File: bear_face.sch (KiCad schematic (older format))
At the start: 276 parts, among them J1 USB_B_Micro, Q1 2N7002, SW1 SW_Push, U1 ATmega32U4-AU, U2 SRV05-4, Y1 16MHz

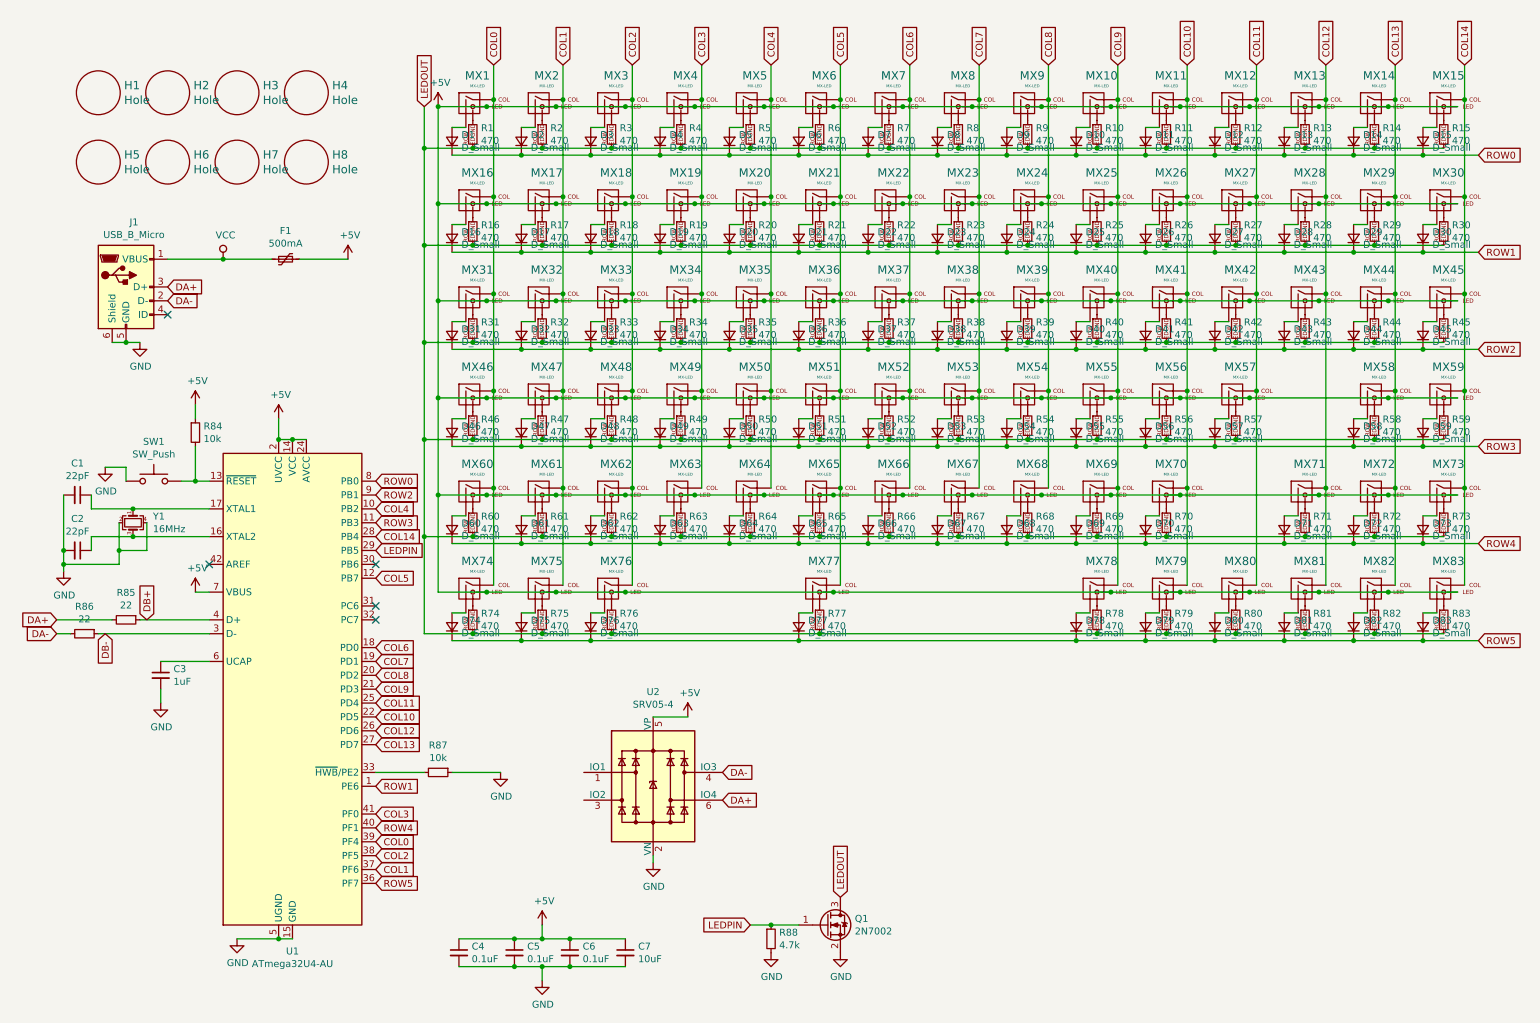
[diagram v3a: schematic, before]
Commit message: AVR ISP pins added, routed
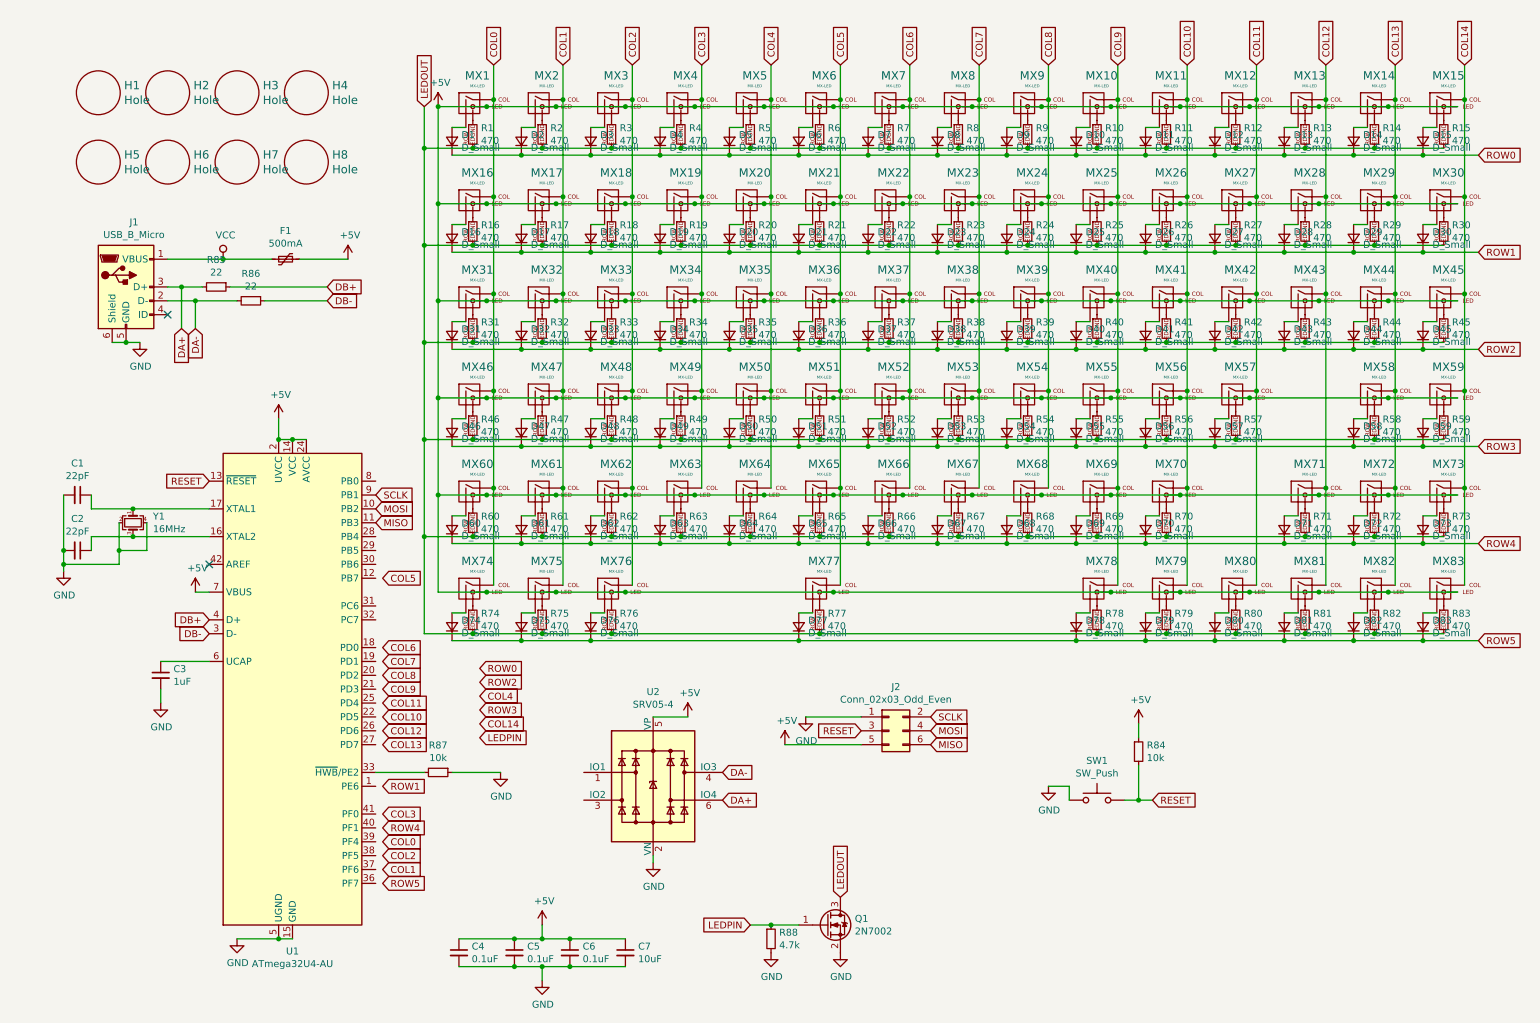
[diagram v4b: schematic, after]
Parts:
- added J2: Conn_02x03_Odd_Even, Connector_PinSocket_2.54mm:PinSocket_2x03_P2.54mm_Vertical, symbol Connector_Generic:Conn_02x03_Odd_Even
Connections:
- net +5V: now also J2.5 (Pin_5)
- net COL0: no longer U1.39 (PF4)
- net COL1: no longer U1.37 (PF6)
- net COL10: no longer U1.22 (PD5)
- net COL11: no longer U1.25 (PD4)
- net COL12: no longer U1.26 (PD6)
- net COL13: no longer U1.27 (PD7)
- net COL14: no longer U1.28 (PB4)
- net COL2: no longer U1.38 (PF5)
- net COL3: no longer U1.41 (PF0)
- net COL4: no longer U1.10 (PB2)
- net COL5: no longer U1.12 (PB7)
- net COL6: no longer U1.18 (PD0)
- net COL7: no longer U1.19 (PD1)
- net COL8: no longer U1.20 (PD2)
- net COL9: no longer U1.21 (PD3)
- net GND: now also J2.1 (Pin_1)
- net LEDPIN: no longer U1.29 (PB5)
- net ROW0: no longer U1.8 (PB0)
- net ROW1: no longer U1.1 (PE6)
- net ROW2: no longer U1.9 (PB1)
- net ROW3: no longer U1.11 (PB3)
- net ROW4: no longer U1.40 (PF1)
- net ROW5: no longer U1.36 (PF7)
- net RESET: now reaches R84.2, SW1.2, U1.13 (~RESET)
- net RESET: now also J2.3 (Pin_3)
- new net MISO: J2.6 (Pin_6), U1.11 (PB3)
- new net MOSI: J2.4 (Pin_4), U1.10 (PB2)
- new net SCLK: J2.2 (Pin_2), U1.9 (PB1)
- no-connect marks 5 -> 2
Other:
- moved on the sheet: R84, R85, R86, SW1
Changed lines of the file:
@@
 	1    0    0    -1
 $EndComp
-Text GLabel 1500 2500 2    50   Input ~ 0
+Text GLabel 1700 2700 3    50   Input ~ 0
 DA-
-Text GLabel 1500 2400 2    50   Input ~ 0
+Text GLabel 1600 2700 3    50   Input ~ 0
 DA+
 $Comp
@@
 L Device:R_Small R85
 U 1 1 5E2BAE37
-P 1200 4800
-F 0 "R85" V 1004 4800 50  0000 C CNN
-F 1 "22" V 1095 4800 50  0000 C CNN
-F 2 "Resistor_SMD:R_0805_2012Metric_Pad1.15x1.40mm_HandSolder" H 1200 4800 50  0001 C CNN
-F 3 "~" H 1200 4800 50  0001 C CNN
-	1    1200 4800
+P 1850 2400
+F 0 "R85" V 1654 2400 50  0000 C CNN
+F 1 "22" V 1745 2400 50  0000 C CNN
+F 2 "Resistor_SMD:R_0805_2012Metric_Pad1.15x1.40mm_HandSolder" H 1850 2400 50  0001 C CNN
+F 3 "~" H 1850 2400 50  0001 C CNN
+	1    1850 2400
 	0    1    1    0
 $EndComp
@@
 L Device:R_Small R86
 U 1 1 5E2BDE9E
-P 900 4900
-F 0 "R86" V 704 4900 50  0000 C CNN
-F 1 "22" V 795 4900 50  0000 C CNN
-F 2 "Resistor_SMD:R_0805_2012Metric_Pad1.15x1.40mm_HandSolder" H 900 4900 50  0001 C CNN
-F 3 "~" H 900 4900 50  0001 C CNN
-	1    900  4900
+P 2100 2500
+F 0 "R86" V 1904 2500 50  0000 C CNN
+F 1 "22" V 1995 2500 50  0000 C CNN
+F 2 "Resistor_SMD:R_0805_2012Metric_Pad1.15x1.40mm_HandSolder" H 2100 2500 50  0001 C CNN
+F 3 "~" H 2100 2500 50  0001 C CNN
+	1    2100 2500
 	0    1    1    0
 $EndComp
-Wire Wire Line
-	800  4900 700  4900
-Wire Wire Line
-	700  4800 1100 4800
 $Comp
 L Device:C_Small C3
@@
 L Switch:SW_Push SW1
 U 1 1 5DFE33D6
-P 1400 3800
-F 0 "SW1" H 1400 4085 50  0000 C CNN
-F 1 "SW_Push" H 1400 3994 50  0000 C CNN
-F 2 "bear_face_parts:PushButton_6x6mm_TH_Pretty" H 1400 4000 50  0001 C CNN
-F 3 "~" H 1400 4000 50  0001 C CNN
-	1    1400 3800
+P 8200 6100
+F 0 "SW1" H 8200 6385 50  0000 C CNN
+F 1 "SW_Push" H 8200 6294 50  0000 C CNN
+F 2 "bear_face_parts:PushButton_6x6mm_TH_Pretty" H 8200 6300 50  0001 C CNN
+F 3 "~" H 8200 6300 50  0001 C CNN
+	1    8200 6100
 	1    0    0    -1
 $EndComp
@@
 	950  4200 950  4300
 Wire Wire Line
-	1600 3800 1700 3800
+	8400 6100 8500 6100
 $Comp
 L power:GND #PWR07
 U 1 1 5E709B12
-P 1050 3700
-F 0 "#PWR07" H 1050 3450 50  0001 C CNN
-F 1 "GND" H 1055 3527 50  0000 C CNN
-F 2 "" H 1050 3700 50  0001 C CNN
-F 3 "" H 1050 3700 50  0001 C CNN
-	1    1050 3700
-	1    0    0    -1
-$EndComp
-Wire Wire Line
-	1050 3700 1200 3700
-Wire Wire Line
-	1200 3700 1200 3800
+P 7850 6000
+F 0 "#PWR07" H 7850 5750 50  0001 C CNN
+F 1 "GND" H 7855 5827 50  0000 C CNN
+F 2 "" H 7850 6000 50  0001 C CNN
+F 3 "" H 7850 6000 50  0001 C CNN
+	1    7850 6000
+	1    0    0    -1
+$EndComp
+Wire Wire Line
+	7850 6000 8000 6000
+Wire Wire Line
+	8000 6000 8000 6100
 $Comp
 L Device:R_Small R84
 U 1 1 5E729BAE
-P 1700 3450
-F 0 "R84" H 1759 3496 50  0000 L CNN
-F 1 "10k" H 1759 3405 50  0000 L CNN
-F 2 "Resistor_SMD:R_0805_2012Metric_Pad1.15x1.40mm_HandSolder" H 1700 3450 50  0001 C CNN
-F 3 "~" H 1700 3450 50  0001 C CNN
-	1    1700 3450
-	1    0    0    -1
-$EndComp
-Wire Wire Line
-	1700 3550 1700 3800
-Connection ~ 1700 3800
-Wire Wire Line
-	1700 3800 1800 3800
+P 8500 5750
+F 0 "R84" H 8559 5796 50  0000 L CNN
+F 1 "10k" H 8559 5705 50  0000 L CNN
+F 2 "Resistor_SMD:R_0805_2012Metric_Pad1.15x1.40mm_HandSolder" H 8500 5750 50  0001 C CNN
+F 3 "~" H 8500 5750 50  0001 C CNN
+	1    8500 5750
+	1    0    0    -1
+$EndComp
+Wire Wire Line
+	8500 5850 8500 6100
+Connection ~ 8500 6100
+Wire Wire Line
+	8500 6100 8600 6100
 $Comp
 L power:+5V #PWR05
 U 1 1 5E749519
-P 1700 3250
-F 0 "#PWR05" H 1700 3100 50  0001 C CNN
-F 1 "+5V" H 1715 3423 50  0000 C CNN
-F 2 "" H 1700 3250 50  0001 C CNN
-F 3 "" H 1700 3250 50  0001 C CNN
-	1    1700 3250
-	1    0    0    -1
-$EndComp
-Wire Wire Line
-	1700 3250 1700 3350
-Text GLabel 700  4800 0    50   Input ~ 0
-DA+
-Text GLabel 700  4900 0    50   Input ~ 0
-DA-
+P 8500 5550
+F 0 "#PWR05" H 8500 5400 50  0001 C CNN
+F 1 "+5V" H 8515 5723 50  0000 C CNN
+F 2 "" H 8500 5550 50  0001 C CNN
+F 3 "" H 8500 5550 50  0001 C CNN
+	1    8500 5550
+	1    0    0    -1
+$EndComp
+Wire Wire Line
+	8500 5550 8500 5650
 $Comp
 L Device:R_Small R87
@@
 	1    0    0    -1
 $EndComp
-Text GLabel 3000 6700 2    50   Input ~ 0
+Text GLabel 3050 6700 2    50   Input ~ 0
 ROW5
-Text GLabel 3000 6200 2    50   Input ~ 0
+Text GLabel 3050 6200 2    50   Input ~ 0
 COL3
 NoConn ~ 1800 4400
-Text GLabel 3000 3800 2    50   Input ~ 0
+Text GLabel 3750 5150 2    50   Input ~ 0
 ROW0
-Text GLabel 3000 6000 2    50   Input ~ 0
+Text GLabel 3050 6000 2    50   Input ~ 0
 ROW1
-Text GLabel 3000 3900 2    50   Input ~ 0
+Text GLabel 3750 5250 2    50   Input ~ 0
 ROW2
-Text GLabel 3000 4100 2    50   Input ~ 0
+Text GLabel 3750 5450 2    50   Input ~ 0
 ROW3
-Text GLabel 3000 4500 2    50   Input ~ 0
+Text GLabel 3050 4500 2    50   Input ~ 0
 COL5
-Text GLabel 3000 5100 2    50   Input ~ 0
+Text GLabel 3050 5100 2    50   Input ~ 0
 COL7
-Text GLabel 3000 5200 2    50   Input ~ 0
+Text GLabel 3050 5200 2    50   Input ~ 0
 COL8
-Text GLabel 3000 5300 2    50   Input ~ 0
+Text GLabel 3050 5300 2    50   Input ~ 0
 COL9
-Text GLabel 3000 5500 2    50   Input ~ 0
+Text GLabel 3050 5500 2    50   Input ~ 0
 COL10
-Text GLabel 3000 5400 2    50   Input ~ 0
+Text GLabel 3050 5400 2    50   Input ~ 0
 COL11
-Text GLabel 3000 5600 2    50   Input ~ 0
+Text GLabel 3050 5600 2    50   Input ~ 0
 COL12
-Text GLabel 3000 5700 2    50   Input ~ 0
+Text GLabel 3050 5700 2    50   Input ~ 0
 COL13
-Text GLabel 3000 4200 2    50   Input ~ 0
+Text GLabel 3750 5550 2    50   Input ~ 0
 COL14
-Text GLabel 3000 4000 2    50   Input ~ 0
+Text GLabel 3750 5350 2    50   Input ~ 0
 COL4
-Text GLabel 3000 5000 2    50   Input ~ 0
+Text GLabel 3050 5000 2    50   Input ~ 0
 COL6
-Text GLabel 3000 6300 2    50   Input ~ 0
+Text GLabel 3050 6300 2    50   Input ~ 0
 ROW4
-Text GLabel 1350 4800 1    50   Input ~ 0
+Text GLabel 2650 2400 2    50   Input ~ 0
 DB+
 Wire Wire Line
 	1700 4600 1800 4600
-Text GLabel 3000 6500 2    50   Input ~ 0
+Text GLabel 3050 6500 2    50   Input ~ 0
 COL2
-Text GLabel 3000 6600 2    50   Input ~ 0
+Text GLabel 3050 6600 2    50   Input ~ 0
 COL1
-Text GLabel 3000 6400 2    50   Input ~ 0
+Text GLabel 3050 6400 2    50   Input ~ 0
 COL0
-Wire Wire Line
-	1000 4900 1800 4900
-Wire Wire Line
-	1300 4800 1800 4800
-NoConn ~ 3000 4400
-NoConn ~ 3000 4700
-NoConn ~ 3000 4800
 NoConn ~ 1500 2600
-Text GLabel 3000 4300 2    50   Input ~ 0
+Text GLabel 3750 5650 2    50   Input ~ 0
 LEDPIN
 Text GLabel 3350 1100 1    50   Input ~ 0
@@
 	1100 2800 1200 2800
 Connection ~ 1200 2800
-Text GLabel 1050 4900 3    50   Input ~ 0
+Text GLabel 2650 2500 2    50   Input ~ 0
 DB-
-Wire Wire Line
-	2500 3500 2400 3500
-Wire Wire Line
-	2400 3500 2300 3500
-Connection ~ 2400 3500
-Connection ~ 2300 3500
-Wire Wire Line
-	2000 7100 2300 7100
-Wire Wire Line
-	2300 7100 2400 7100
-Connection ~ 2300 7100
 Wire Wire Line
 	2300 3350 2300 3500
@@
 Text GLabel 5700 7000 0    50   Input ~ 0
 LEDPIN
+Wire Wire Line
+	1500 2500 1700 2500
+Wire Wire Line
+	1950 2400 2650 2400
+Wire Wire Line
+	2200 2500 2650 2500
+Wire Wire Line
+	1500 2400 1600 2400
+Wire Wire Line
+	1600 2700 1600 2400
+Connection ~ 1600 2400
+Wire Wire Line
+	1600 2400 1750 2400
+Wire Wire Line
+	1700 2700 1700 2500
+Connection ~ 1700 2500
+Wire Wire Line
+	1700 2500 2000 2500
+Text GLabel 1800 4800 0    50   Input ~ 0
+DB+
+Text GLabel 1800 4900 0    50   Input ~ 0
+DB-
+Wire Wire Line
+	2300 7100 2400 7100
+Wire Wire Line
+	2000 7100 2300 7100
+Connection ~ 2300 7100
+Connection ~ 2300 3500
+Wire Wire Line
+	2400 3500 2300 3500
+Wire Wire Line
+	2500 3500 2400 3500
+Connection ~ 2400 3500
 $Comp
 L MCU_Microchip_ATmega:ATmega32U4-AU U1
@@
 	1    0    0    -1
 $EndComp
+Text GLabel 3000 3900 2    50   Input ~ 0
+SCLK
+Text GLabel 3000 4000 2    50   Input ~ 0
+MOSI
+Text GLabel 3000 4100 2    50   Input ~ 0
+MISO
+$Comp
+L Connector_Generic:Conn_02x03_Odd_Even J2
+U 1 1 5E38C6F7
+P 6700 5600
+F 0 "J2" H 6750 5917 50  0000 C CNN
+F 1 "Conn_02x03_Odd_Even" H 6750 5826 50  0000 C CNN
+F 2 "Connector_PinSocket_2.54mm:PinSocket_2x03_P2.54mm_Vertical" H 6700 5600 50  0001 C CNN
+F 3 "~" H 6700 5600 50  0001 C CNN
+	1    6700 5600
+	1    0    0    -1
+$EndComp
+Text GLabel 7000 5500 2    50   Input ~ 0
+SCLK
+Text GLabel 7000 5600 2    50   Input ~ 0
+MOSI
+Text GLabel 7000 5700 2    50   Input ~ 0
+MISO
+Text GLabel 8600 6100 2    50   Input ~ 0
+RESET
+Text GLabel 1800 3800 0    50   Input ~ 0
+RESET
+Text GLabel 6500 5600 0    50   Input ~ 0
+RESET
+Wire Wire Line
+	6500 5500 6100 5500
+$Comp
+L power:GND #PWR0105
+U 1 1 5E4F520E
+P 6100 5500
+F 0 "#PWR0105" H 6100 5250 50  0001 C CNN
+F 1 "GND" H 6105 5327 50  0000 C CNN
+F 2 "" H 6100 5500 50  0001 C CNN
+F 3 "" H 6100 5500 50  0001 C CNN
+	1    6100 5500
+	1    0    0    -1
+$EndComp
+Wire Wire Line
+	6500 5700 5950 5700
+$Comp
+L power:+5V #PWR0106
+U 1 1 5E54EE72
+P 5950 5700
+F 0 "#PWR0106" H 5950 5550 50  0001 C CNN
+F 1 "+5V" H 5965 5873 50  0000 C CNN
+F 2 "" H 5950 5700 50  0001 C CNN
+F 3 "" H 5950 5700 50  0001 C CNN
+	1    5950 5700
+	1    0    0    -1
+$EndComp
